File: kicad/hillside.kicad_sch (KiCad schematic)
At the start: 83 parts, among them J1 Haptic, J2 TRRS, J3 Bat_Pos, J4 Bat_GND, K1 SW_Key, K10 SW_Key, K11 SW_Key, K12 SW_Key, K13 SW_Key, K14 SW_Key, K15 SW_Key, K16 SW_Key, K17 SW_Key, K18 SW_Key, K19 SW_Key, K2 SW_Key, K20 SW_Rotary, K21 SW_Key, K22 SW_Key, K23 SW_Key, K24 SW_Key, K3 SW_Key, K4 SW_Key, K5 SW_Key, K6 SW_Key, K7 SW_Key, K8 SW_Key, K9 SW_Key, SW1 Reset, SW2 SW_Power, U1 ProMicro_r

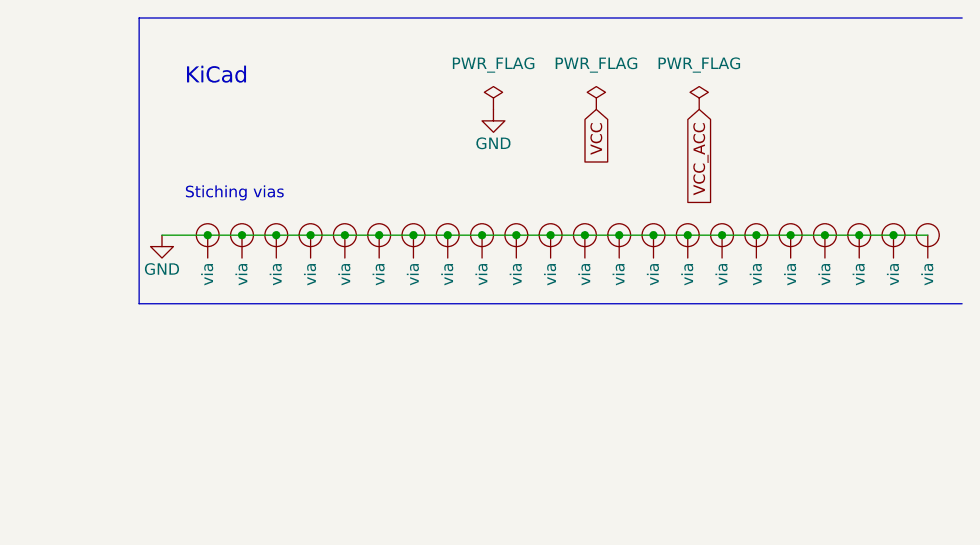
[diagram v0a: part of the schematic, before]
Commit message: Remove stitching vias now handled by islands
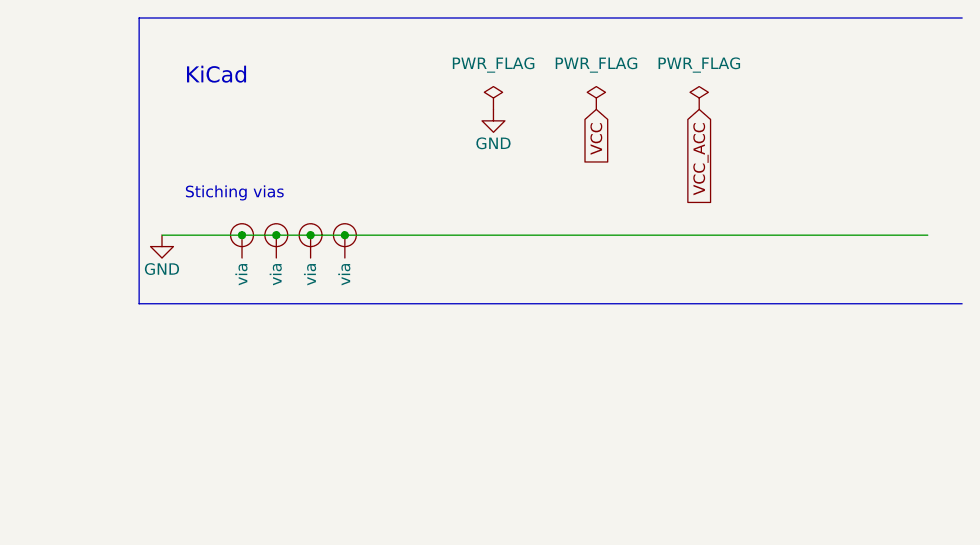
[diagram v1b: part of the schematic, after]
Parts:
- removed V1, V10, V11, V12, V13, V14, V15, V16, V17, V18, V19, V20, V21, V22, V6, V7, V8, V9: Via, hillside_basic:VIA-0.8mm, symbol hillside_basic:Via

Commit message: Use KiCad lib mounting holes and jumper cutoff pad
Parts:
- H4, H5, H8, H9: footprint hillside_basic:MountingHole_2.2mm_M2_Pad -> MountingHole:MountingHole_2.2mm_M2_Pad
- H6, H7: footprint hillside_basic:MountingHole_2.2mm_M2 -> MountingHole:MountingHole_2.2mm_M2
- JP1: footprint hillside_basic:SolderJumper-2_P1.3mm_Bridged_RoundedPad1.0x1.5mm -> Jumper:SolderJumper-2_P1.3mm_Bridged_RoundedPad1.0x1.5mm
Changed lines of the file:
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@@
     (property "Reference" "JP1" (id 0) (at 175.26 114.3 0))
     (property "Value" "SolderJumper" (id 1) (at 175.26 116.84 0))
-    (property "Footprint" "hillside_basic:SolderJumper-2_P1.3mm_Bridged_RoundedPad1.0x1.5mm" (id 2) (at 175.26 120.65 0)
+    (property "Footprint" "Jumper:SolderJumper-2_P1.3mm_Bridged_RoundedPad1.0x1.5mm" (id 2) (at 175.26 120.65 0)
       (effects (font (size 1.27 1.27)) hide)
     )
@@
       (effects (font (size 1.27 1.27)) (justify left))
     )
-    (property "Footprint" "hillside_basic:MountingHole_2.2mm_M2_Pad" (id 2) (at 248.92 125.73 0)
+    (property "Footprint" "MountingHole:MountingHole_2.2mm_M2_Pad" (id 2) (at 248.92 125.73 0)
       (effects (font (size 1.27 1.27)) hide)
     )
@@
       (effects (font (size 1.27 1.27)) (justify left))
     )
-    (property "Footprint" "hillside_basic:MountingHole_2.2mm_M2" (id 2) (at 248.92 130.81 0)
+    (property "Footprint" "MountingHole:MountingHole_2.2mm_M2" (id 2) (at 248.92 130.81 0)
       (effects (font (size 1.27 1.27)) hide)
     )
@@
       (effects (font (size 1.27 1.27)) (justify left))
     )
-    (property "Footprint" "hillside_basic:MountingHole_2.2mm_M2_Pad" (id 2) (at 231.14 125.73 0)
+    (property "Footprint" "MountingHole:MountingHole_2.2mm_M2_Pad" (id 2) (at 231.14 125.73 0)
       (effects (font (size 1.27 1.27)) hide)
     )
@@
       (effects (font (size 1.27 1.27)) (justify left))
     )
-    (property "Footprint" "hillside_basic:MountingHole_2.2mm_M2" (id 2) (at 231.14 130.81 0)
+    (property "Footprint" "MountingHole:MountingHole_2.2mm_M2" (id 2) (at 231.14 130.81 0)
       (effects (font (size 1.27 1.27)) hide)
     )
@@
       (effects (font (size 1.27 1.27)) (justify left))
     )
-    (property "Footprint" "hillside_basic:MountingHole_2.2mm_M2_Pad" (id 2) (at 231.14 135.89 0)
+    (property "Footprint" "MountingHole:MountingHole_2.2mm_M2_Pad" (id 2) (at 231.14 135.89 0)
       (effects (font (size 1.27 1.27)) hide)
     )
@@
       (effects (font (size 1.27 1.27)) (justify left))
     )
-    (property "Footprint" "hillside_basic:MountingHole_2.2mm_M2_Pad" (id 2) (at 248.92 135.89 0)
+    (property "Footprint" "MountingHole:MountingHole_2.2mm_M2_Pad" (id 2) (at 248.92 135.89 0)
       (effects (font (size 1.27 1.27)) hide)
     )
@@
     )
     (path "/00000000-0000-0000-0000-00006219aac2"
-      (reference "H4") (unit 1) (value "MountHole") (footprint "hillside_basic:MountingHole_2.2mm_M2_Pad")
+      (reference "H4") (unit 1) (value "MountHole") (footprint "MountingHole:MountingHole_2.2mm_M2_Pad")
     )
     (path "/00000000-0000-0000-0000-000062184c57"
-      (reference "H5") (unit 1) (value "MountHole") (footprint "hillside_basic:MountingHole_2.2mm_M2_Pad")
+      (reference "H5") (unit 1) (value "MountHole") (footprint "MountingHole:MountingHole_2.2mm_M2_Pad")
     )
     (path "/00000000-0000-0000-0000-00006219aacc"
-      (reference "H6") (unit 1) (value "MountHole") (footprint "hillside_basic:MountingHole_2.2mm_M2")
+      (reference "H6") (unit 1) (value "MountHole") (footprint "MountingHole:MountingHole_2.2mm_M2")
     )
     (path "/00000000-0000-0000-0000-00006218a790"
-      (reference "H7") (unit 1) (value "MountHole") (footprint "hillside_basic:MountingHole_2.2mm_M2")
+      (reference "H7") (unit 1) (value "MountHole") (footprint "MountingHole:MountingHole_2.2mm_M2")
     )
     (path "/00000000-0000-0000-0000-0000621ecfae"
-      (reference "H8") (unit 1) (value "MountHole") (footprint "hillside_basic:MountingHole_2.2mm_M2_Pad")
+      (reference "H8") (unit 1) (value "MountHole") (footprint "MountingHole:MountingHole_2.2mm_M2_Pad")
     )
     (path "/00000000-0000-0000-0000-0000621fdcbf"
-      (reference "H9") (unit 1) (value "MountHole") (footprint "hillside_basic:MountingHole_2.2mm_M2_Pad")
+      (reference "H9") (unit 1) (value "MountHole") (footprint "MountingHole:MountingHole_2.2mm_M2_Pad")
     )
     (path "/00000000-0000-0000-0000-0000616b8147"
@@
     )
     (path "/00000000-0000-0000-0000-000061a8564f"
-      (reference "JP1") (unit 1) (value "SolderJumper") (footprint "hillside_basic:SolderJumper-2_P1.3mm_Bridged_RoundedPad1.0x1.5mm")
+      (reference "JP1") (unit 1) (value "SolderJumper") (footprint "Jumper:SolderJumper-2_P1.3mm_Bridged_RoundedPad1.0x1.5mm")
     )
     (path "/00000000-0000-0000-0000-0000617cbce8"
